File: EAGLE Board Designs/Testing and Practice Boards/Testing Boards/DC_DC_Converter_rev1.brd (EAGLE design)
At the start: 99.9 x 58.7 mm, 9 parts, among them U1 DCM3714BD2K13E0C09

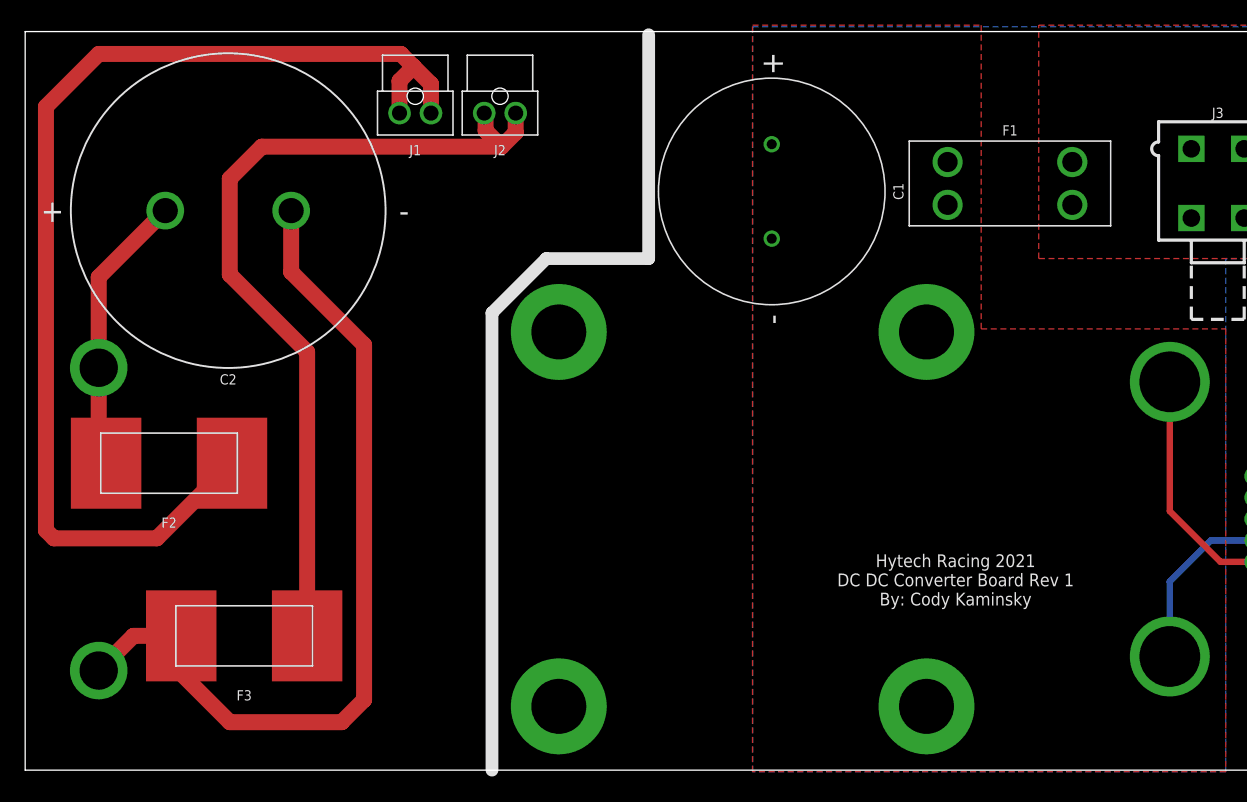
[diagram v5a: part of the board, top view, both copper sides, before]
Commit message: Added a silkscreen to the board
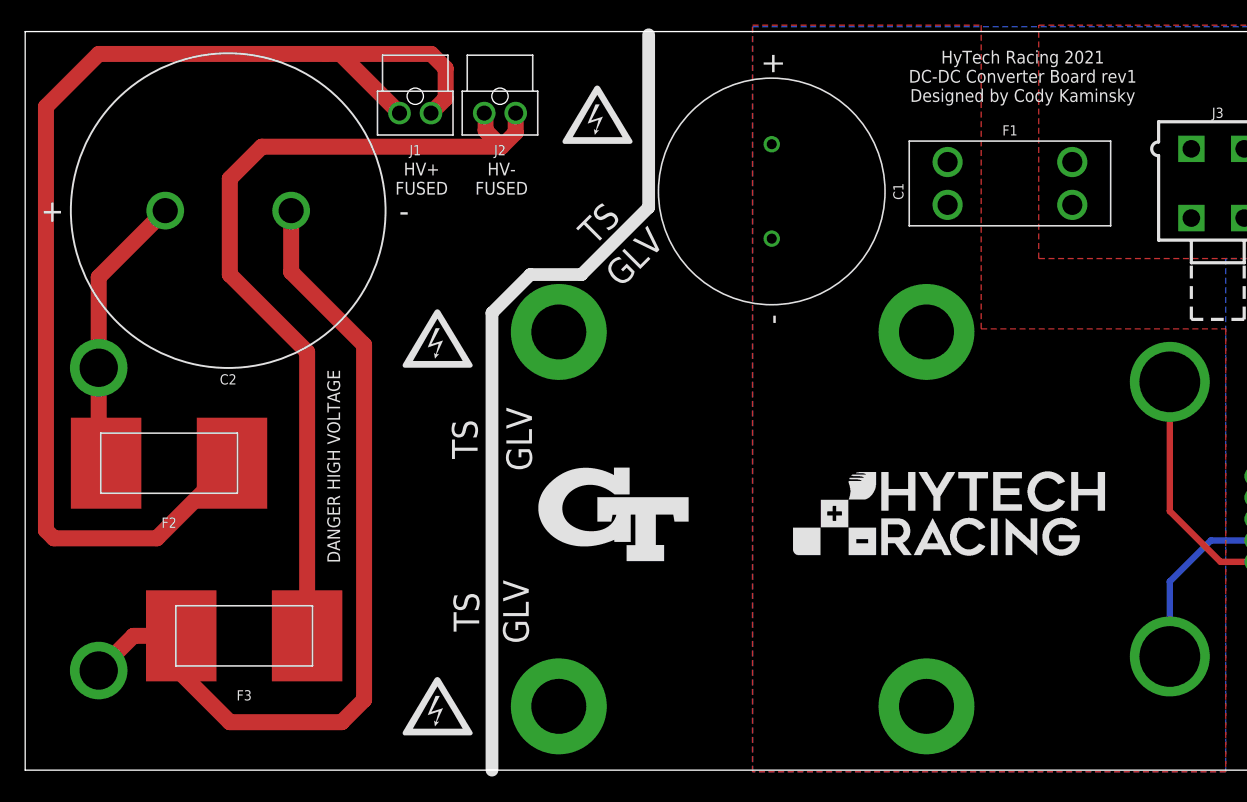
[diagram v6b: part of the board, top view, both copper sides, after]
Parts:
- added U$1, U$10, U$2, U$3, U$8, U$9: (no value), HyTechAesthetics:HV_0.50"
- added U$6: (no value), HyTechAesthetics:LOGO_HYTECH_1.0"
- added U$7: (no value), HyTechAesthetics:LOGO_GT_0.50"
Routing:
- net HV+: track 90.9 -> 95.8 mm
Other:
- board text added: "DANGER HIGH VOLTAGE"
- board text added: "GLV"
- board text added: "HV+ FUSED"
- board text added: "HV- FUSED"
- board text added: "HyTech Racing 2021 DC-DC Converter Board rev1 Designed by Cody Kaminsky"
- board text added: "TS"
- board text removed: "Hytech Racing 2021 DC DC Converter Board Rev 1 By: Cody Kaminsky"
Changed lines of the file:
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@@
 <drawing>
 <settings>
-<setting alwaysvectorfont="no"/>
+<setting alwaysvectorfont="yes"/>
 <setting verticaltext="up"/>
 </settings>
@@
 <dimension x1="2.794" y1="58.725" x2="2.794" y2="-0.127" x3="-7.62" y3="29.299" textsize="1.778" layer="1"/>
 <dimension x1="1.524" y1="39.624" x2="1.524" y2="58.547" x3="0" y3="49.0855" textsize="1.778" layer="1"/>
-<text x="76.708" y="13.081" size="1.016" layer="21" font="vector" align="bottom-center">Hytech Racing 2021
-DC DC Converter Board Rev 1
-By: Cody Kaminsky</text>
-<wire x1="39.878" y1="0" x2="39.878" y2="36.322" width="1.016" layer="21"/>
-<wire x1="39.878" y1="36.322" x2="44.196" y2="40.64" width="1.016" layer="21"/>
-<wire x1="44.196" y1="40.64" x2="52.324" y2="40.64" width="1.016" layer="21"/>
-<wire x1="52.324" y1="40.64" x2="52.324" y2="58.42" width="1.016" layer="21"/>
+<text x="82.042" y="53.086" size="1.016" layer="21" font="vector" align="bottom-center">HyTech Racing 2021
+DC-DC Converter Board rev1
+Designed by Cody Kaminsky</text>
 <dimension x1="42.672" y1="52.324" x2="52.578" y2="47.879" x3="47.4693125" y3="49.754540625" textsize="1.778" layer="156"/>
 <dimension x1="30.48" y1="33.274" x2="41.275" y2="33.528" x3="35.858525" y3="34.207378125" textsize="1.778" layer="156"/>
 <dimension x1="40.767" y1="48.895" x2="44.196" y2="38.735" x3="40.2097875" y3="43.048296875" textsize="1.778" layer="156"/>
 <dimension x1="30.353" y1="5.715" x2="40.894" y2="5.08" x3="35.7750375" y3="7.913071875" textsize="1.778" layer="156"/>
+<wire x1="39.878" y1="0" x2="39.878" y2="36.322" width="1.016" layer="21"/>
+<wire x1="42.926" y1="39.37" x2="46.99" y2="39.37" width="1.016" layer="21"/>
+<wire x1="46.99" y1="39.37" x2="52.324" y2="44.704" width="1.016" layer="21"/>
+<wire x1="52.324" y1="44.704" x2="52.324" y2="58.42" width="1.016" layer="21"/>
+<dimension x1="41.783" y1="49.657" x2="49.149" y2="42.545" x3="45.967121875" y3="46.620021875" textsize="1.778" layer="156"/>
+<dimension x1="40.767" y1="48.895" x2="44.831" y2="40.259" x3="43.673609375" y3="44.98858125" textsize="1.778" layer="156"/>
+<wire x1="39.878" y1="36.322" x2="42.926" y2="39.37" width="1.016" layer="21"/>
+<wire x1="39.878" y1="0" x2="39.878" y2="36.322" width="1.016" layer="22"/>
+<wire x1="39.878" y1="36.322" x2="42.926" y2="39.37" width="1.016" layer="22"/>
+<wire x1="42.926" y1="39.37" x2="46.99" y2="39.37" width="1.016" layer="22"/>
+<wire x1="46.99" y1="39.37" x2="52.324" y2="44.704" width="1.016" layer="22"/>
+<wire x1="52.324" y1="44.704" x2="52.324" y2="58.42" width="1.016" layer="22"/>
+<text x="34.29" y="45.72" size="1.016" layer="21" font="vector" ratio="12" align="bottom-center">HV+
+FUSED</text>
+<text x="40.64" y="45.72" size="1.016" layer="21" font="vector" ratio="12" align="bottom-center">HV-
+FUSED</text>
+<text x="27.305" y="24.13" size="1.016" layer="21" font="vector" ratio="12" rot="R90" align="center">DANGER HIGH VOLTAGE</text>
+<text x="27.305" y="24.13" size="1.016" layer="22" font="vector" ratio="12" rot="MR90" align="center">DANGER HIGH VOLTAGE</text>
+<text x="37.846" y="12.573" size="2.032" layer="21" font="vector" rot="R90" align="center">TS</text>
+<text x="37.719" y="26.289" size="2.032" layer="21" font="vector" rot="R90" align="center">TS</text>
+<text x="48.387" y="43.434" size="2.032" layer="21" font="vector" rot="R225" align="center">TS</text>
+<text x="48.387" y="43.434" size="2.032" layer="22" font="vector" rot="MR135" align="center">TS</text>
+<text x="37.719" y="26.289" size="2.032" layer="22" font="vector" rot="MR270" align="center">TS</text>
+<text x="37.846" y="12.573" size="2.032" layer="22" font="vector" rot="MR270" align="center">TS</text>
+<text x="41.783" y="12.573" size="2.032" layer="21" font="vector" rot="R270" align="center">GLV</text>
+<text x="42.037" y="26.289" size="2.032" layer="21" font="vector" rot="R270" align="center">GLV</text>
+<text x="51.181" y="40.767" size="2.032" layer="21" font="vector" rot="R225" align="center">GLV</text>
+<text x="51.181" y="40.767" size="2.032" layer="22" font="vector" rot="MR135" align="center">GLV</text>
+<text x="42.037" y="26.289" size="2.032" layer="22" font="vector" rot="MR90" align="center">GLV</text>
+<text x="41.783" y="12.573" size="2.032" layer="22" font="vector" rot="MR90" align="center">GLV</text>
+<text x="19.05" y="51.435" size="1.016" layer="22" font="vector" ratio="12" rot="MR0" align="center">DANGER HIGH VOLTAGE</text>
 </plain>
 <attributes>
@@
 <attribute name="NAME" x="18.923" y="31.45" size="0.8128" layer="25" font="vector" rot="R180" align="bottom-center"/>
 </element>
+<element name="U$1" library="HyTechAesthetics" package="HV_0.50&quot;" value="" x="35.56" y="5.08" smashed="yes"/>
+<element name="U$2" library="HyTechAesthetics" package="HV_0.50&quot;" value="" x="35.56" y="34.29" smashed="yes"/>
+<element name="U$3" library="HyTechAesthetics" package="HV_0.50&quot;" value="" x="48.26" y="52.07" smashed="yes"/>
+<element name="U$6" library="HyTechAesthetics" package="LOGO_HYTECH_1.0&quot;" value="" x="63.5" y="16.764" smashed="yes"/>
+<element name="U$7" library="HyTechAesthetics" package="LOGO_GT_0.50&quot;" value="" x="49.53" y="20.32" smashed="yes"/>
+<element name="U$8" library="HyTechAesthetics" package="HV_0.50&quot;" value="" x="35.56" y="5.08" smashed="yes" rot="MR0"/>
+<element name="U$9" library="HyTechAesthetics" package="HV_0.50&quot;" value="" x="35.56" y="34.29" smashed="yes" rot="MR0"/>
+<element name="U$10" library="HyTechAesthetics" package="HV_0.50&quot;" value="" x="48.26" y="52.07" smashed="yes" rot="MR0"/>
 </elements>
 <signals>
@@
 <wire x1="5.08" y1="18.415" x2="4.445" y2="19.05" width="1.27" layer="1"/>
 <wire x1="4.445" y1="19.05" x2="4.445" y2="52.705" width="1.27" layer="1"/>
-<wire x1="8.636" y1="56.896" x2="4.445" y2="52.705" width="1.27" layer="1"/>
-<wire x1="32.639" y1="56.896" x2="8.636" y2="56.896" width="1.27" layer="1"/>
-<wire x1="32.532" y1="52.197" x2="32.532" y2="54.757" width="1.27" layer="1"/>
-<wire x1="33.655" y1="55.88" x2="32.532" y2="54.757" width="1.27" layer="1"/>
-<wire x1="35.032" y1="52.197" x2="35.032" y2="54.503" width="1.27" layer="1"/>
-<wire x1="35.032" y1="54.503" x2="33.655" y2="55.88" width="1.27" layer="1"/>
-<wire x1="33.655" y1="55.88" x2="32.639" y2="56.896" width="1.27" layer="1"/>
+<wire x1="4.445" y1="52.705" x2="8.636" y2="56.896" width="1.27" layer="1"/>
+<wire x1="35.052" y1="56.896" x2="36.195" y2="55.753" width="1.27" layer="1"/>
+<wire x1="36.195" y1="55.753" x2="36.195" y2="53.36" width="1.27" layer="1"/>
+<wire x1="8.636" y1="56.896" x2="26.67" y2="56.896" width="1.27" layer="1"/>
+<wire x1="27.833" y1="56.896" x2="35.052" y2="56.896" width="1.27" layer="1"/>
+<wire x1="36.195" y1="53.36" x2="35.032" y2="52.197" width="1.27" layer="1"/>
+<wire x1="27.833" y1="56.896" x2="26.67" y2="56.896" width="1.27" layer="1"/>
+<wire x1="32.532" y1="52.197" x2="27.833" y2="56.896" width="1.27" layer="1"/>
 </signal>
 <signal name="HV-">

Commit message: Made final changes
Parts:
- moved J1 3.17 mm to (33.8, 55.4), turned to 180 degrees
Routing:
- net HV+: track 95.8 -> 86.3 mm
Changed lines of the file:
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@@
 </class>
 </classes>
-<designrules name="default">
-<description language="de">&lt;b&gt;EAGLE Design Rules&lt;/b&gt;
-&lt;p&gt;
-Die Standard-Design-Rules sind so gewählt, dass sie für
-die meisten Anwendungen passen. Sollte ihre Platine
-besondere Anforderungen haben, treffen Sie die erforderlichen
-Einstellungen hier und speichern die Design Rules unter
-einem neuen Namen ab.</description>
-<description language="en">&lt;b&gt;EAGLE Design Rules&lt;/b&gt;
+<designrules name="JLCPCB (2 Layer)">
+<description language="en">&lt;b&gt;JLCPCB Design Rules (2 Layers)&lt;/b&gt;
 &lt;p&gt;
 The default Design Rules have been set to cover
-a wide range of applications. Your particular design
-may have different requirements, so please make the
-necessary adjustments and save your customized
-design rules under a new name.</description>
+a wide range of applications.
+&lt;p&gt;
+Source: &lt;a href=&quot;https://jlcpcb.com/capabilities/Capabilities&quot;&gt;JLCPCB&lt;/a&gt;
+&lt;/p&gt;</description>
 <param name="layerSetup" value="(1*16)"/>
 <param name="mtCopper" value="0.035mm 0.035mm 0.035mm 0.035mm 0.035mm 0.035mm 0.035mm 0.035mm 0.035mm 0.035mm 0.035mm 0.035mm 0.035mm 0.035mm 0.035mm 0.035mm"/>
-<param name="mtIsolate" value="1.5mm 0.15mm 0.2mm 0.15mm 0.2mm 0.15mm 0.2mm 0.15mm 0.2mm 0.15mm 0.2mm 0.15mm 0.2mm 0.15mm 0.2mm"/>
-<param name="mdWireWire" value="6mil"/>
-<param name="mdWirePad" value="6mil"/>
-<param name="mdWireVia" value="6mil"/>
-<param name="mdPadPad" value="6mil"/>
-<param name="mdPadVia" value="6mil"/>
-<param name="mdViaVia" value="6mil"/>
-<param name="mdSmdPad" value="6mil"/>
-<param name="mdSmdVia" value="6mil"/>
-<param name="mdSmdSmd" value="6mil"/>
+<param name="mtIsolate" value="1.53mm 0.15mm 0.2mm 0.15mm 0.2mm 0.15mm 0.2mm 0.15mm 0.2mm 0.15mm 0.2mm 0.15mm 0.2mm 0.15mm 0.2mm"/>
+<param name="mdWireWire" value="5mil"/>
+<param name="mdWirePad" value="5mil"/>
+<param name="mdWireVia" value="8mil"/>
+<param name="mdPadPad" value="5mil"/>
+<param name="mdPadVia" value="10mil"/>
+<param name="mdViaVia" value="20mil"/>
+<param name="mdSmdPad" value="5mil"/>
+<param name="mdSmdVia" value="10mil"/>
+<param name="mdSmdSmd" value="5mil"/>
 <param name="mdViaViaSameLayer" value="6mil"/>
 <param name="mnLayersViaInSmd" value="2"/>
-<param name="mdCopperDimension" value="40mil"/>
-<param name="mdDrill" value="6mil"/>
+<param name="mdCopperDimension" value="0.2mm"/>
+<param name="mdDrill" value="21mil"/>
 <param name="mdSmdStop" value="0mil"/>
-<param name="msWidth" value="6mil"/>
-<param name="msDrill" value="0.35mm"/>
+<param name="msWidth" value="5mil"/>
+<param name="msDrill" value="0.3mm"/>
 <param name="msMicroVia" value="9.99mm"/>
 <param name="msBlindViaRatio" value="0.5"/>
@@
 <param name="rvViaOuter" value="0.25"/>
 <param name="rvViaInner" value="0.25"/>
-<param name="rvMicroViaOuter" value="0.25"/>
-<param name="rvMicroViaInner" value="0.25"/>
-<param name="rlMinPadTop" value="10mil"/>
+<param name="rvMicroViaOuter" value="0"/>
+<param name="rvMicroViaInner" value="0"/>
+<param name="rlMinPadTop" value="6mil"/>
 <param name="rlMaxPadTop" value="20mil"/>
-<param name="rlMinPadInner" value="10mil"/>
+<param name="rlMinPadInner" value="6mil"/>
 <param name="rlMaxPadInner" value="20mil"/>
-<param name="rlMinPadBottom" value="10mil"/>
+<param name="rlMinPadBottom" value="6mil"/>
 <param name="rlMaxPadBottom" value="20mil"/>
-<param name="rlMinViaOuter" value="8mil"/>
-<param name="rlMaxViaOuter" value="20mil"/>
-<param name="rlMinViaInner" value="8mil"/>
-<param name="rlMaxViaInner" value="20mil"/>
-<param name="rlMinMicroViaOuter" value="4mil"/>
+<param name="rlMinViaOuter" value="6mil"/>
+<param name="rlMaxViaOuter" value="12mil"/>
+<param name="rlMinViaInner" value="6mil"/>
+<param name="rlMaxViaInner" value="12mil"/>
+<param name="rlMinMicroViaOuter" value="6mil"/>
 <param name="rlMaxMicroViaOuter" value="20mil"/>
-<param name="rlMinMicroViaInner" value="4mil"/>
+<param name="rlMinMicroViaInner" value="6mil"/>
 <param name="rlMaxMicroViaInner" value="20mil"/>
 <param name="psTop" value="-1"/>
 <param name="psBottom" value="-1"/>
-<param name="psFirst" value="-1"/>
+<param name="psFirst" value="0"/>
 <param name="psElongationLong" value="100"/>
 <param name="psElongationOffset" value="100"/>
 <param name="mvStopFrame" value="1"/>
 <param name="mvCreamFrame" value="0"/>
-<param name="mlMinStopFrame" value="4mil"/>
-<param name="mlMaxStopFrame" value="4mil"/>
+<param name="mlMinStopFrame" value="6mil"/>
+<param name="mlMaxStopFrame" value="6mil"/>
 <param name="mlMinCreamFrame" value="0mil"/>
 <param name="mlMaxCreamFrame" value="0mil"/>
-<param name="mlViaStopLimit" value="0mil"/>
+<param name="mlViaStopLimit" value="30mil"/>
 <param name="srRoundness" value="0"/>
 <param name="srMinRoundness" value="0mil"/>
@@
 <param name="checkRestrict" value="1"/>
 <param name="checkStop" value="0"/>
-<param name="checkValues" value="0"/>
+<param name="checkValues" value="1"/>
 <param name="checkNames" value="1"/>
 <param name="checkWireStubs" value="1"/>
-<param name="checkPolygonWidth" value="0"/>
+<param name="checkPolygonWidth" value="1"/>
 <param name="useDiameter" value="13"/>
 <param name="maxErrors" value="50"/>
@@
 </autorouter>
 <elements>
-<element name="U1" library="HyTechDevices" package="3714DCM_VIA" value="DCM3714BD2K13E0C09" x="8.636" y="19.939" smashed="yes" rot="MR180">
-<attribute name="NAME" x="3.556" y="-0.381" size="0.8128" layer="26" font="vector" rot="MR180"/>
-</element>
+<element name="U1" library="HyTechDevices" package="3714DCM_VIA" value="DCM3714BD2K13E0C09" x="8.636" y="19.939" smashed="yes" rot="MR180"/>
 <element name="C1" library="HyTechDevices" package="EKYC*MM" value="4.7 mF" x="62.103" y="45.974" smashed="yes" rot="R90">
 <attribute name="NAME" x="72.569" y="45.974" size="0.8128" layer="25" font="vector" rot="R90" align="bottom-center"/>
@@
 <attribute name="NAME" x="81.026" y="50.419" size="0.8128" layer="25" font="vector" align="bottom-center"/>
 </element>
-<element name="J1" library="HyTechDevices" package="MOLEX_NANOFIT_PTH_02" value="" x="33.782" y="52.197" smashed="yes">
-<attribute name="MPN" value="1053091202" x="33.782" y="52.197" size="1.778" layer="27" display="off"/>
-<attribute name="NAME" x="33.782" y="49.657" size="0.8128" layer="25" font="vector" rot="R180" align="bottom-center"/>
+<element name="J1" library="HyTechDevices" package="MOLEX_NANOFIT_PTH_02" value="" x="33.782" y="55.372" smashed="yes" rot="R180">
+<attribute name="MPN" value="1053091202" x="33.782" y="55.372" size="1.778" layer="27" rot="R180" display="off"/>
+<attribute name="NAME" x="33.782" y="49.784" size="0.8128" layer="25" font="vector" rot="R180" align="bottom-center"/>
 </element>
 <element name="J2" library="HyTechDevices" package="MOLEX_NANOFIT_PTH_02" value="" x="40.513" y="52.197" smashed="yes">
@@
 <wire x1="5.08" y1="18.415" x2="4.445" y2="19.05" width="1.27" layer="1"/>
 <wire x1="4.445" y1="19.05" x2="4.445" y2="52.705" width="1.27" layer="1"/>
-<wire x1="4.445" y1="52.705" x2="8.636" y2="56.896" width="1.27" layer="1"/>
-<wire x1="35.052" y1="56.896" x2="36.195" y2="55.753" width="1.27" layer="1"/>
-<wire x1="36.195" y1="55.753" x2="36.195" y2="53.36" width="1.27" layer="1"/>
-<wire x1="8.636" y1="56.896" x2="26.67" y2="56.896" width="1.27" layer="1"/>
-<wire x1="27.833" y1="56.896" x2="35.052" y2="56.896" width="1.27" layer="1"/>
-<wire x1="36.195" y1="53.36" x2="35.032" y2="52.197" width="1.27" layer="1"/>
-<wire x1="27.833" y1="56.896" x2="26.67" y2="56.896" width="1.27" layer="1"/>
-<wire x1="32.532" y1="52.197" x2="27.833" y2="56.896" width="1.27" layer="1"/>
+<wire x1="8.636" y1="56.896" x2="4.445" y2="52.705" width="1.27" layer="1"/>
+<wire x1="32.532" y1="55.372" x2="31.008" y2="56.896" width="1.27" layer="1"/>
+<wire x1="31.008" y1="56.896" x2="8.636" y2="56.896" width="1.27" layer="1"/>
+<wire x1="35.032" y1="55.372" x2="33.508" y2="56.896" width="1.27" layer="1"/>
+<wire x1="33.508" y1="56.896" x2="31.008" y2="56.896" width="1.27" layer="1"/>
 </signal>
 <signal name="HV-">
@@
 <wire x1="41.763" y1="52.197" x2="41.763" y2="50.653" width="1.27" layer="1"/>
 <wire x1="41.763" y1="50.653" x2="40.64" y2="49.53" width="1.27" layer="1"/>
-<wire x1="19.05" y1="46.99" x2="21.59" y2="49.53" width="1.27" layer="1"/>
-<wire x1="21.59" y1="49.53" x2="40.64" y2="49.53" width="1.27" layer="1"/>
+<wire x1="19.05" y1="46.99" x2="20.32" y2="48.26" width="1.27" layer="1"/>
+<wire x1="39.37" y1="48.26" x2="40.64" y2="49.53" width="1.27" layer="1"/>
+<wire x1="20.32" y1="48.26" x2="39.37" y2="48.26" width="1.27" layer="1"/>
 </signal>
 <signal name="+12V">
@@
 <mfgpreviewcolor name="substratecolor" color="0xFF786E46"/>
 </mfgpreviewcolors>
+<errors>
+</errors>
 </board>
 </drawing>

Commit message: Final changes made
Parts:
- moved U$6 0.40 mm to (63.4, 16.4)
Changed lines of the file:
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@@
 <element name="U$2" library="HyTechAesthetics" package="HV_0.50&quot;" value="" x="35.56" y="34.29" smashed="yes"/>
 <element name="U$3" library="HyTechAesthetics" package="HV_0.50&quot;" value="" x="48.26" y="52.07" smashed="yes"/>
-<element name="U$6" library="HyTechAesthetics" package="LOGO_HYTECH_1.0&quot;" value="" x="63.5" y="16.764" smashed="yes"/>
+<element name="U$6" library="HyTechAesthetics" package="LOGO_HYTECH_1.0&quot;" value="" x="63.373" y="16.383" smashed="yes"/>
 <element name="U$7" library="HyTechAesthetics" package="LOGO_GT_0.50&quot;" value="" x="49.53" y="20.32" smashed="yes"/>
 <element name="U$8" library="HyTechAesthetics" package="HV_0.50&quot;" value="" x="35.56" y="5.08" smashed="yes" rot="MR0"/>
